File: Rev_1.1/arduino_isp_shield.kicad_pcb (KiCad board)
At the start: 2 copper layers, 53.3 x 31.8 mm, 9 parts, among them J1 ISP, J2 Conn_01x08, J3 Conn_01x10, U1 ATTINY13/15/25/45/85, U2 ATTINY24/44/84, U3 ATTINY2313/4313

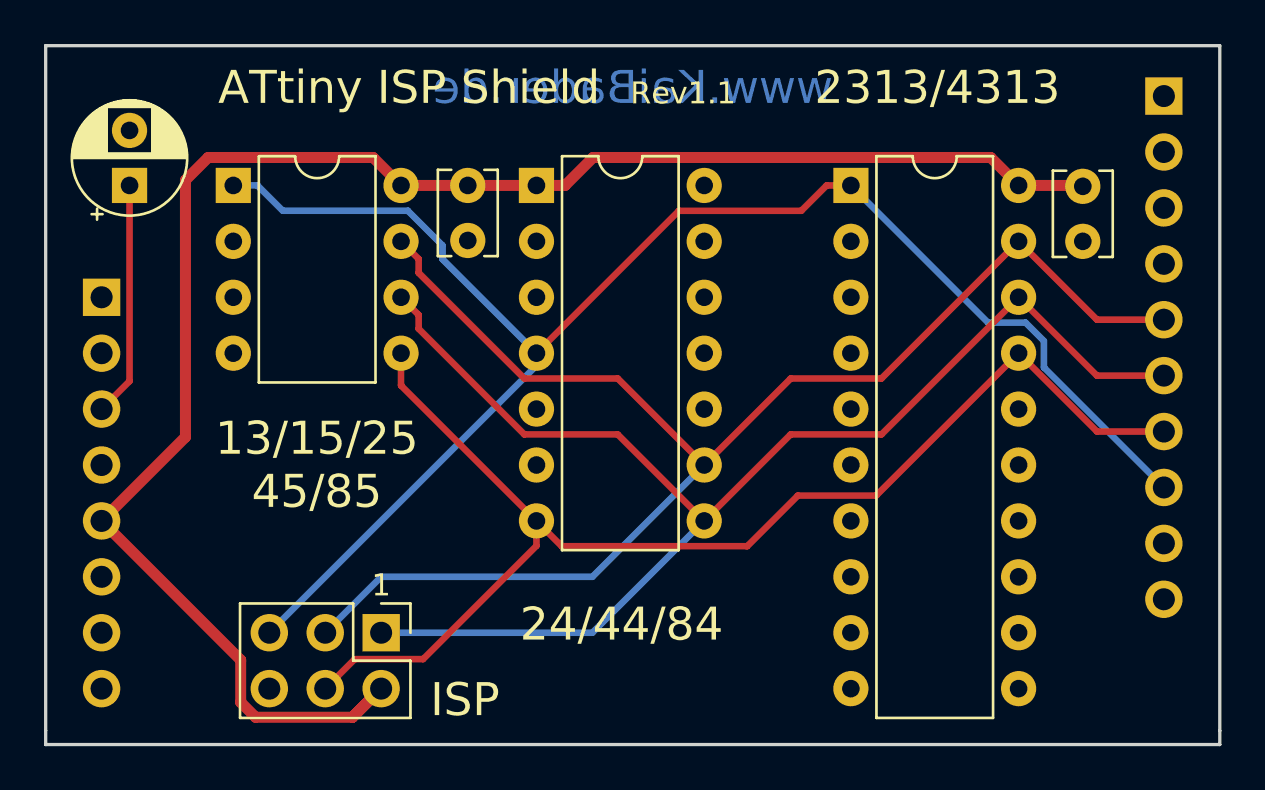
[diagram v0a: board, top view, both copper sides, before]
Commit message: Minor adaptions: improved the alignment of some traces.
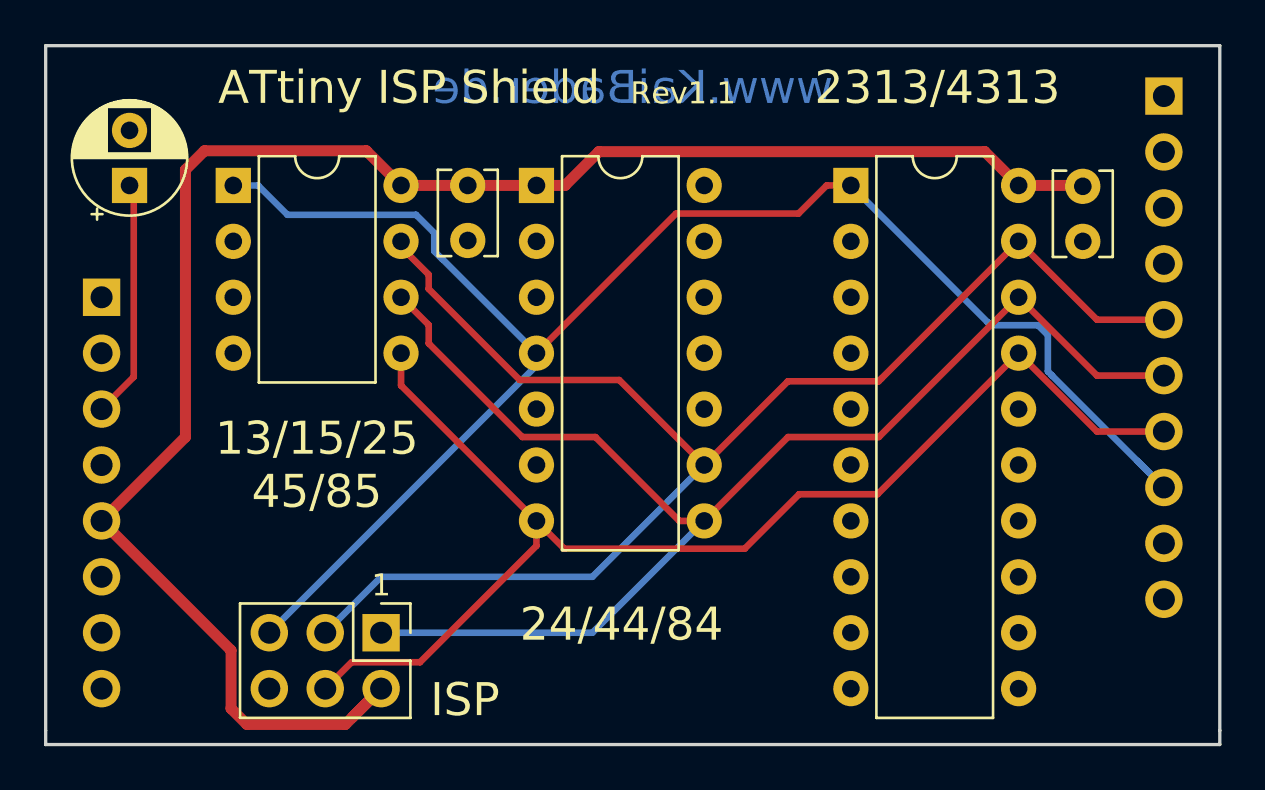
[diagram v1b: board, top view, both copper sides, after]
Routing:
- net /~RESET: track 73.1 -> 75.2 mm
- net +5V: track 79.7 -> 81.2 mm
- net Net-(C4-Pad1): track 10.7 -> 11.5 mm
